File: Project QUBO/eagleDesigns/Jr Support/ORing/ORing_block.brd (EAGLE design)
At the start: 96.5 x 72.1 mm, 83 parts

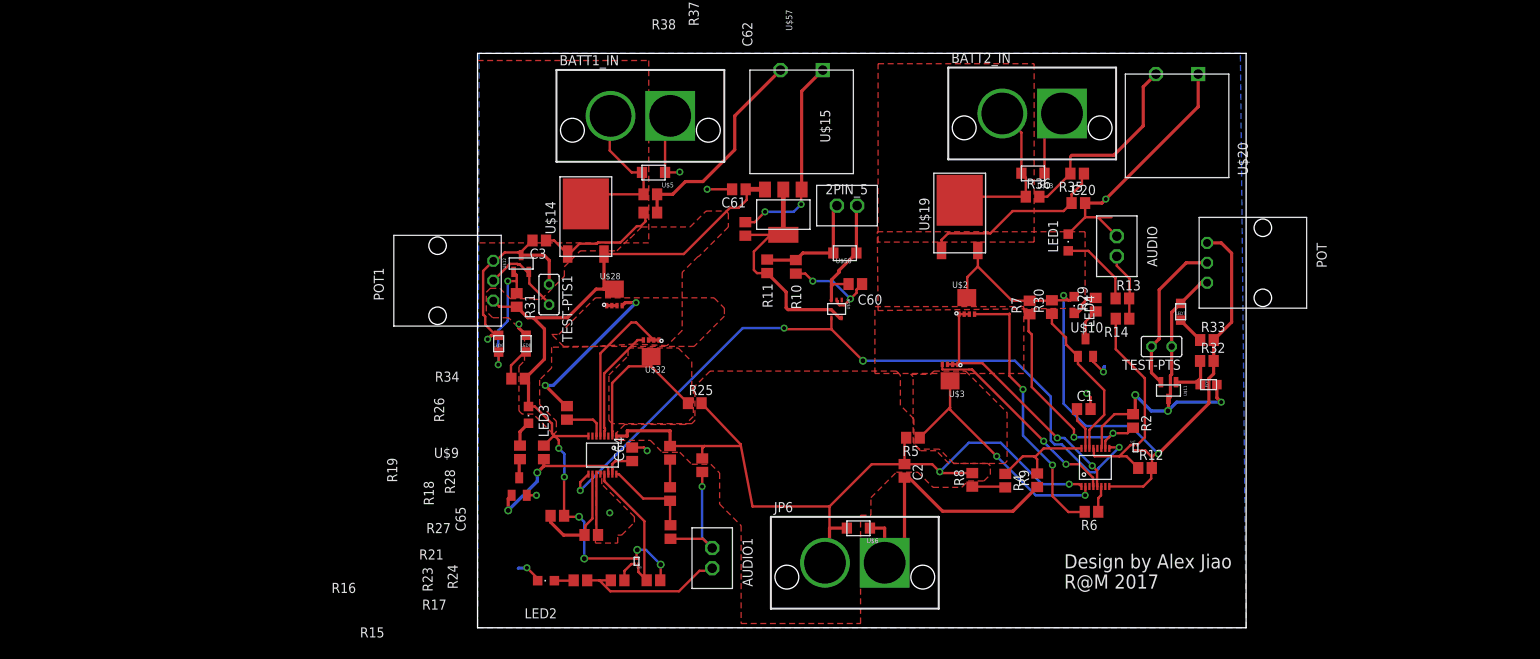
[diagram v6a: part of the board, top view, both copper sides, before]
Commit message: finishing touches on oring board
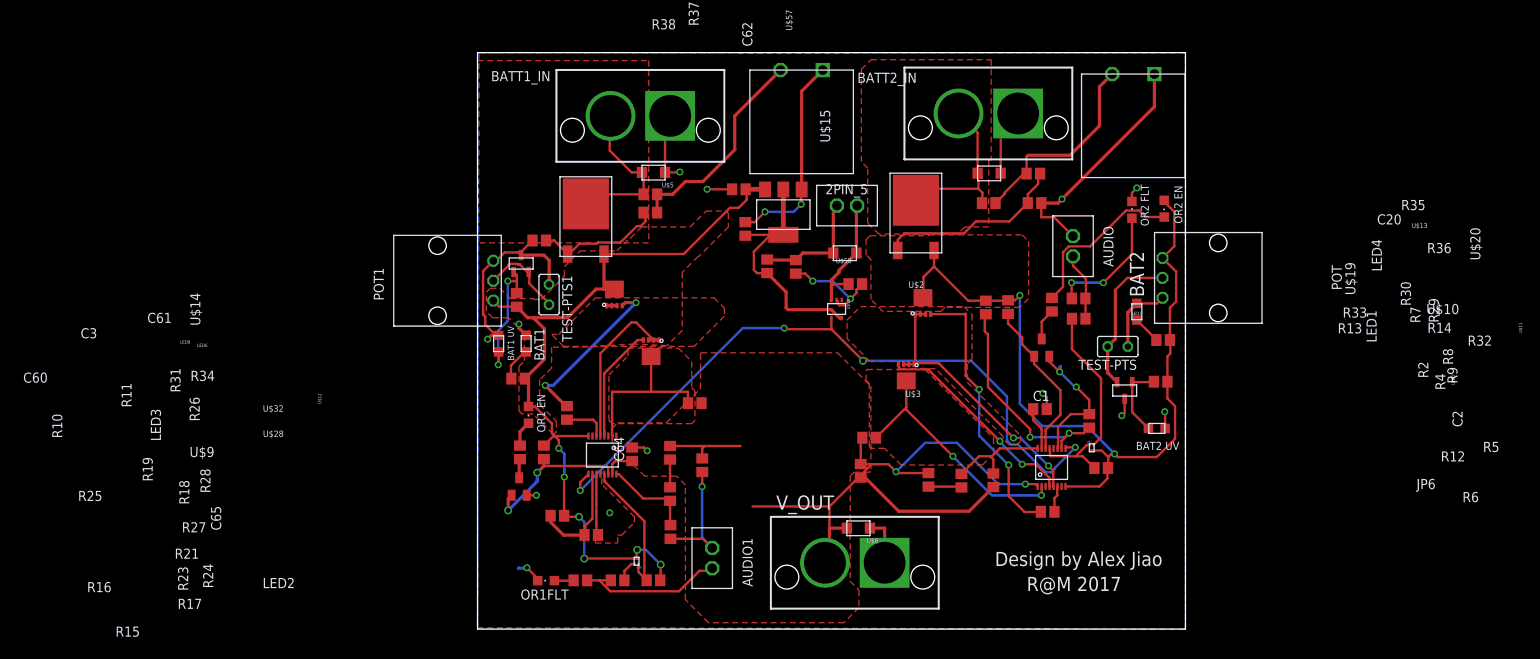
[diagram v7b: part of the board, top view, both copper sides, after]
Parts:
- R12: value (none) -> 20k+
- moved LED4 16.6 mm to (86.2, 52.8)
- moved LED1 8.99 mm to (82.2, 52.6)
- moved LED5 8.51 mm to (85.3, 25.2)
- moved R32 6.36 mm to (85.8, 31.1)
- moved POT 5.91 mm to (86.0, 44.1)
- moved R36 5.56 mm to (64.2, 53.5)
- moved AUDIO 5.50 mm to (74.8, 48.1)
- moved BATT2_IN 5.50 mm to (64.2, 64.8)
- moved C1 5.50 mm to (70.6, 27.6)
- moved C2 5.50 mm to (48.1, 19.9)
- moved C20 5.50 mm to (70.0, 53.5)
- moved LED7 5.50 mm to (82.8, 39.9)
- moved R12 5.50 mm to (78.3, 20.2)
- moved R13 5.50 mm to (75.5, 41.5)
- moved R14 5.50 mm to (75.5, 39.0)
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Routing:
- net GND: track 229.3 -> 200.4 mm, vias 17 -> 18
- net V_BATT: track 101.2 -> 72.5 mm
- net N$27: track 3.86 -> 21.8 mm
- net V_BATT2: track 94.0 -> 100.6 mm
- net N$16: track 9.92 -> 15.6 mm, vias 0 -> 2
- net N$14: track 93.4 -> 87.9 mm
- net N$30: track 5.99 -> 9.40 mm
- net N$45: track 20.2 -> 22.2 mm
- net N$23: track 19.9 -> 19.0 mm
- net N$60: track 20.2 -> 21.0 mm
- added copper zone on layer 1, net N$2
- removed copper zone on layer 1, net V_BATT2
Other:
- board size 96.5 x 72.1 mm -> 88.9 x 72.4 mm
- board text added: "BAT1"
- board text added: "BAT1 UV"
- board text added: "BAT2"
- board text added: "BAT2 UV"
- board text added: "OR1 EN"
- board text added: "OR1FLT"
- board text added: "OR2 EN"
- board text added: "OR2 FLT"
- board text added: "V_OUT"
